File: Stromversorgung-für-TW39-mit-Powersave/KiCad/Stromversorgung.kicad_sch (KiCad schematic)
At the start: 15 parts, among them J1 230V~ IN, J2 RP, J3 +5V, J4 230V~ OUT, J5 +90V, K1 FINDER-40.52, Q1 BC337, T1 GERTH 422.60.2

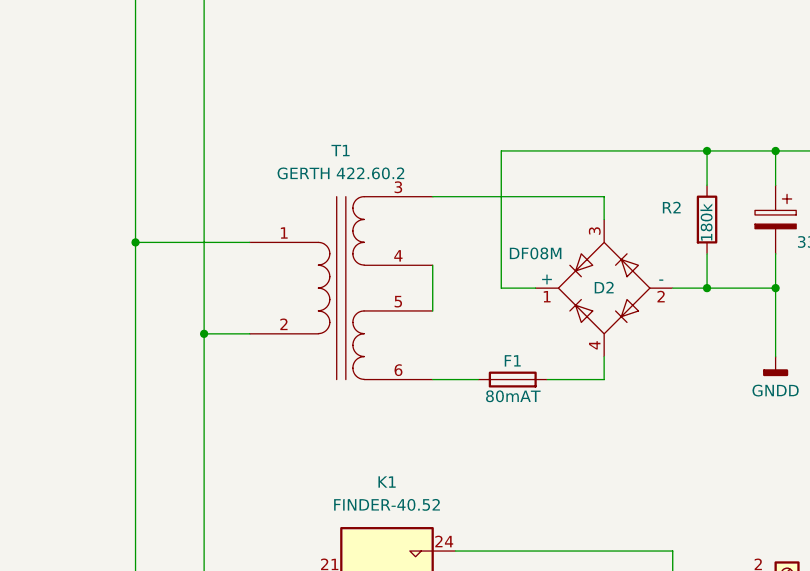
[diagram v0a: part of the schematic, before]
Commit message: bugfix in KiCad
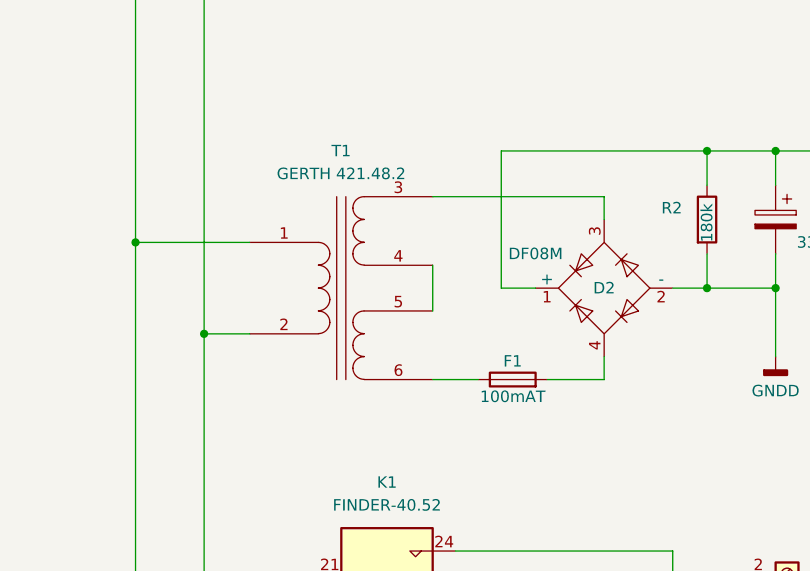
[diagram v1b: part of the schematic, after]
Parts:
- F1: value 80mAT -> 100mAT
- T1: value GERTH 422.60.2 -> GERTH 421.48.2
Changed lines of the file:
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@@
 			)
 		)
-		(property "Value" "GERTH 422.60.2"
+		(property "Value" "GERTH 421.48.2"
 			(at 121.92 71.12 0)
 			(effects
@@
 			)
 		)
-		(property "Value" "80mAT"
+		(property "Value" "100mAT"
 			(at 140.97 95.885 90)
 			(effects
